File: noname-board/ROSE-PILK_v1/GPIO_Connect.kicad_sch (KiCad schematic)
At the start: 2 parts, among them J11 Conn_02x11_Row_Letter_First, J12 Conn_02x20_Row_Letter_First

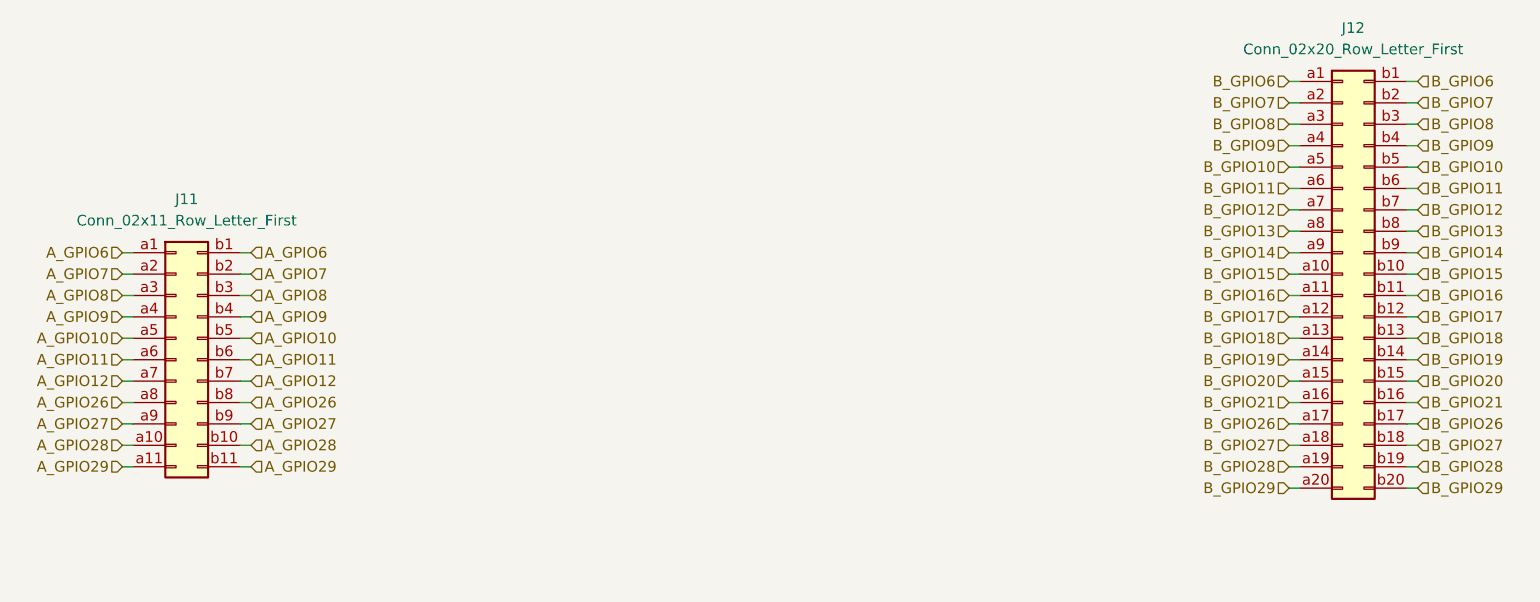
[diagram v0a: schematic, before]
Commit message: schematic finished, placement progress
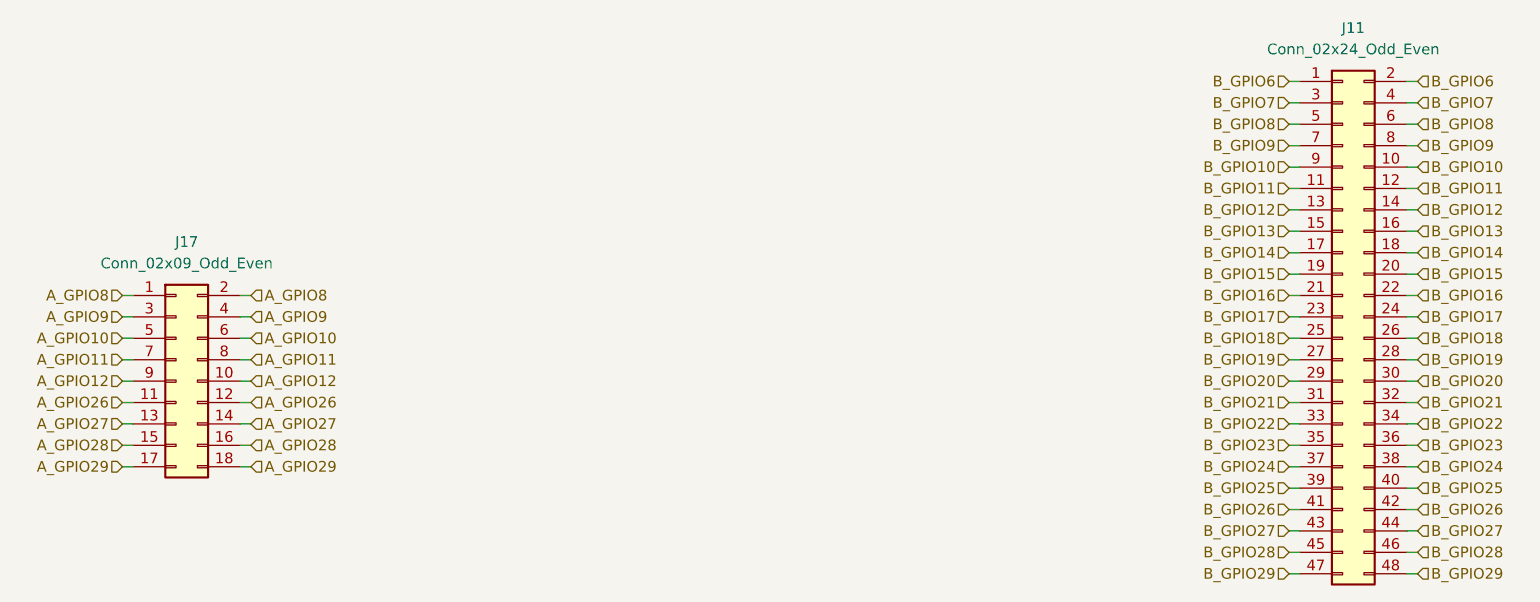
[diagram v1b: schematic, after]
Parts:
- removed J11: Conn_02x11_Row_Letter_First, Connector_PinHeader_1.27mm:PinHeader_2x11_P1.27mm_Vertical, symbol Connector_Generic:Conn_02x11_Row_Letter_First
- removed J12: Conn_02x20_Row_Letter_First, Connector_PinHeader_1.27mm:PinHeader_2x20_P1.27mm_Vertical, symbol Connector_Generic:Conn_02x20_Row_Letter_First
- added J11: Conn_02x24_Odd_Even, Connector_PinHeader_2.00mm:PinHeader_2x24_P2.00mm_Vertical, symbol Connector_Generic:Conn_02x24_Odd_Even
- added J17: Conn_02x09_Odd_Even, Connector_PinHeader_2.00mm:PinHeader_2x09_P2.00mm_Vertical, symbol Connector_Generic:Conn_02x09_Odd_Even
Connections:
- net A_GPIO10: now also J17.5 (Pin_5), J17.6 (Pin_6)
- net A_GPIO11: now also J17.7 (Pin_7), J17.8 (Pin_8)
- net A_GPIO12: now also J17.10 (Pin_10), J17.9 (Pin_9)
- net A_GPIO26: now also J17.11 (Pin_11), J17.12 (Pin_12)
- net A_GPIO27: now also J17.13 (Pin_13), J17.14 (Pin_14)
- net A_GPIO28: now also J17.15 (Pin_15), J17.16 (Pin_16)
- net A_GPIO29: now also J17.17 (Pin_17), J17.18 (Pin_18)
- net A_GPIO8: now also J17.1 (Pin_1), J17.2 (Pin_2)
- net A_GPIO9: now also J17.3 (Pin_3), J17.4 (Pin_4)
- net B_GPIO10: now also J11.10 (Pin_10), J11.9 (Pin_9)
- net B_GPIO11: now also J11.11 (Pin_11), J11.12 (Pin_12)
- net B_GPIO12: now also J11.13 (Pin_13), J11.14 (Pin_14)
- net B_GPIO13: now also J11.15 (Pin_15), J11.16 (Pin_16)
- net B_GPIO14: now also J11.17 (Pin_17), J11.18 (Pin_18)
- net B_GPIO15: now also J11.19 (Pin_19), J11.20 (Pin_20)
- net B_GPIO16: now also J11.21 (Pin_21), J11.22 (Pin_22)
- net B_GPIO17: now also J11.23 (Pin_23), J11.24 (Pin_24)
- net B_GPIO18: now also J11.25 (Pin_25), J11.26 (Pin_26)
- net B_GPIO19: now also J11.27 (Pin_27), J11.28 (Pin_28)
- net B_GPIO20: now also J11.29 (Pin_29), J11.30 (Pin_30)
- net B_GPIO21: now also J11.31 (Pin_31), J11.32 (Pin_32)
- net B_GPIO26: now also J11.41 (Pin_41), J11.42 (Pin_42)
- net B_GPIO27: now also J11.43 (Pin_43), J11.44 (Pin_44)
- net B_GPIO28: now also J11.45 (Pin_45), J11.46 (Pin_46)
- net B_GPIO29: now also J11.47 (Pin_47), J11.48 (Pin_48)
- net B_GPIO6: now also J11.1 (Pin_1), J11.2 (Pin_2)
- net B_GPIO7: now also J11.3 (Pin_3), J11.4 (Pin_4)
- net B_GPIO8: now also J11.5 (Pin_5), J11.6 (Pin_6)
- net B_GPIO9: now also J11.7 (Pin_7), J11.8 (Pin_8)
- new net B_GPIO22: J11.33 (Pin_33), J11.34 (Pin_34)
- new net B_GPIO23: J11.35 (Pin_35), J11.36 (Pin_36)
- new net B_GPIO24: J11.37 (Pin_37), J11.38 (Pin_38)
- new net B_GPIO25: J11.39 (Pin_39), J11.40 (Pin_40)
